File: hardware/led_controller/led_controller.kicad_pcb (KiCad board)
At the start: 2 copper layers, 50 x 70 mm, 31 parts, among them J1 Header, J2 Header, J3 Header, J4 Header, J5 POWER, J6 Conn_01x02, U1 74AHCT125, U3 Waveshare ESP32-S3/C6 Zero

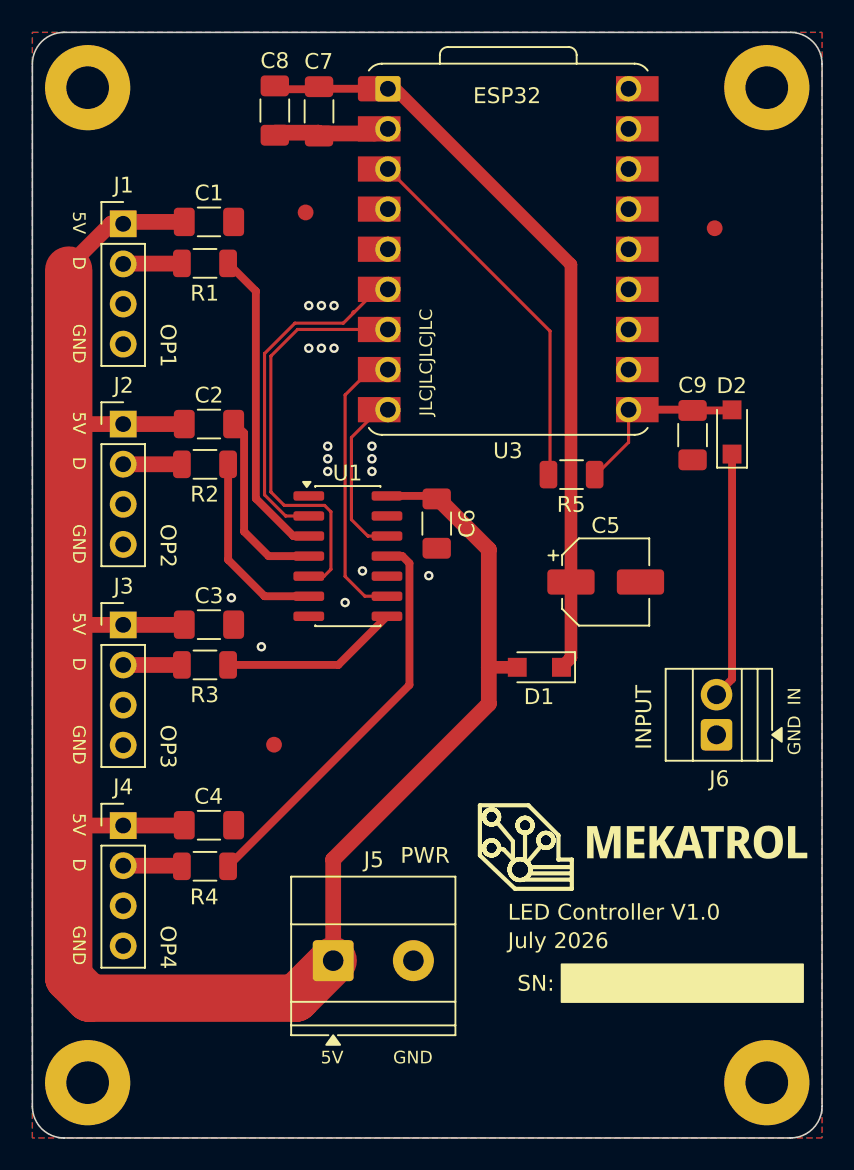
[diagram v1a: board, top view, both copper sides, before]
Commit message: Use new KICAD API in scripts
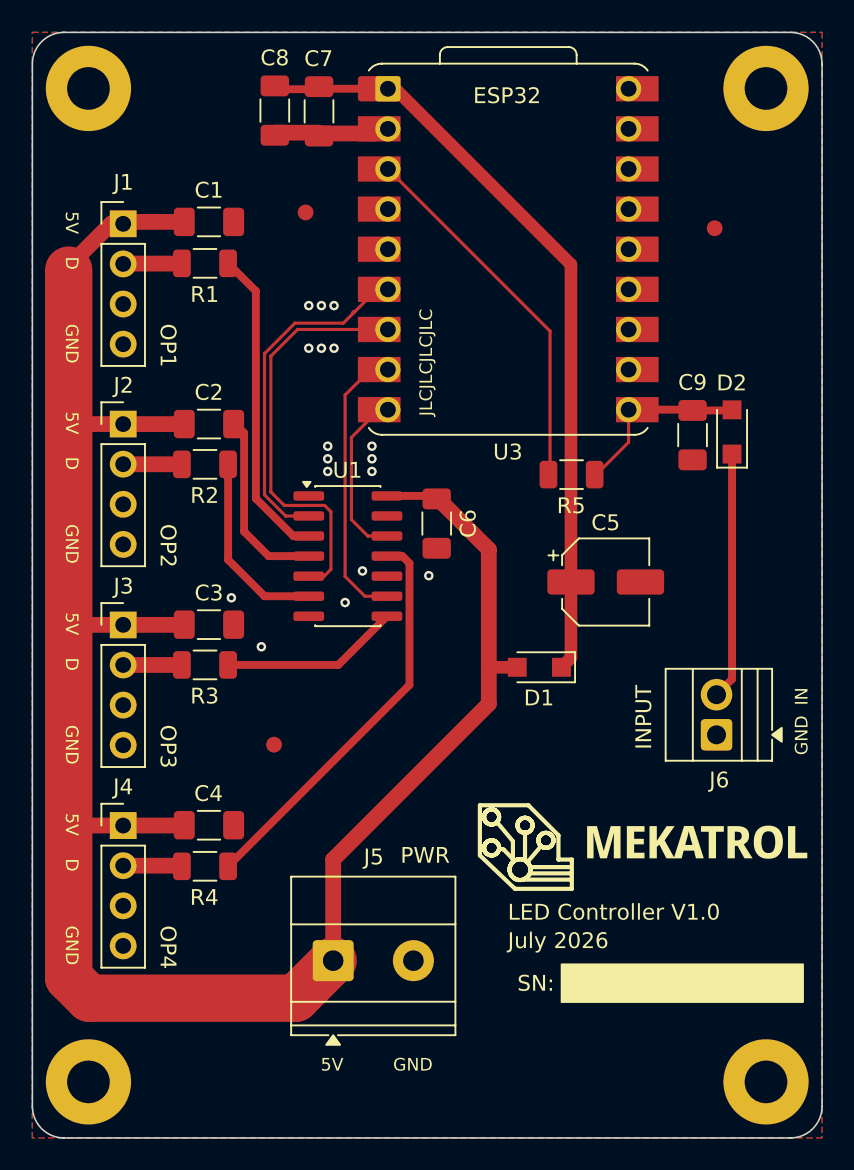
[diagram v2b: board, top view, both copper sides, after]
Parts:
- moved H2 0.07 mm to (166.4, 53.5)
- moved H4 0.07 mm to (166.4, 116.5)
- moved H1 0.07 mm to (123.5, 53.5)
- moved H3 0.07 mm to (123.5, 116.5)

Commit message: Updated center sprit to distibute as well
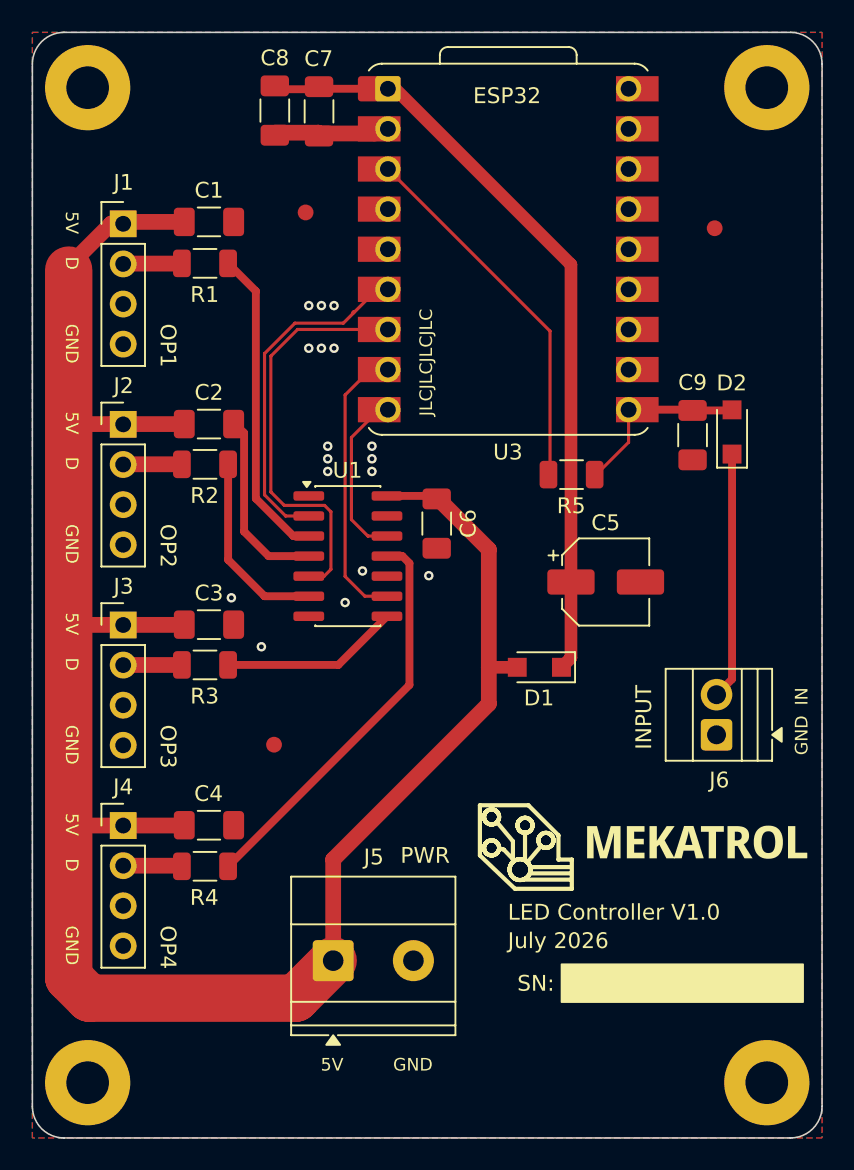
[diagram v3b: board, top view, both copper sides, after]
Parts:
- moved H2 0.07 mm to (166.5, 53.5)
- moved H4 0.07 mm to (166.5, 116.5)
- moved H1 0.07 mm to (123.5, 53.5)
- moved H3 0.07 mm to (123.5, 116.5)
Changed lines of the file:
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@@
 	(footprint "MountingHole:MountingHole_2.7mm_M2.5_Pad"
 		(layer "F.Cu")
-		(at 166.45 116.45)
+		(at 166.5 116.5)
 		(descr "Mounting Hole 2.7mm, M2.5, generated by kicad-footprint-generator mountinghole.py")
 		(tags "mountinghole M2.5")
@@
 	(footprint "Connector_PinHeader_2.54mm:PinHeader_1x04_P2.54mm_Vertical"
 		(layer "F.Cu")
-		(at 125.75 74.8)
+		(at 125.75 74.82)
 		(descr "Through hole straight pin header, 1x04, 2.54mm pitch, single row")
 		(tags "Through hole pin header THT 1x04 2.54mm single row")
@@
 		(sheetname "/")
 		(sheetfile "led_controller.kicad_sch")
-		(units
-			(unit
-				(name "A")
-				(pins "1" "2" "3" "4")
-			)
-		)
 		(attr through_hole)
 		(duplicate_pad_numbers_are_jumpers no)
@@
 	(footprint "MountingHole:MountingHole_2.7mm_M2.5_Pad"
 		(layer "F.Cu")
-		(at 166.45 53.55)
+		(at 166.5 53.5)
 		(descr "Mounting Hole 2.7mm, M2.5, generated by kicad-footprint-generator mountinghole.py")
 		(tags "mountinghole M2.5")
@@
 		(sheetname "/")
 		(sheetfile "led_controller.kicad_sch")
-		(units
-			(unit
-				(name "A")
-				(pins "1" "2" "3" "4")
-			)
-		)
 		(attr through_hole)
 		(duplicate_pad_numbers_are_jumpers no)
@@
 	(footprint "Connector_PinHeader_2.54mm:PinHeader_1x04_P2.54mm_Vertical"
 		(layer "F.Cu")
-		(at 125.75 87.513333)
+		(at 125.75 87.520001)
 		(descr "Through hole straight pin header, 1x04, 2.54mm pitch, single row")
 		(tags "Through hole pin header THT 1x04 2.54mm single row")
@@
 		(sheetname "/")
 		(sheetfile "led_controller.kicad_sch")
-		(units
-			(unit
-				(name "A")
-				(pins "1" "2" "3" "4")
-			)
-		)
 		(attr through_hole)
 		(duplicate_pad_numbers_are_jumpers no)
@@
 	(footprint "MountingHole:MountingHole_2.7mm_M2.5_Pad"
 		(layer "F.Cu")
-		(at 123.55 53.55)
+		(at 123.5 53.5)
 		(descr "Mounting Hole 2.7mm, M2.5, generated by kicad-footprint-generator mountinghole.py")
 		(tags "mountinghole M2.5")
@@
 	(footprint "MountingHole:MountingHole_2.7mm_M2.5_Pad"
 		(layer "F.Cu")
-		(at 123.55 116.45)
+		(at 123.5 116.5)
 		(descr "Mounting Hole 2.7mm, M2.5, generated by kicad-footprint-generator mountinghole.py")
 		(tags "mountinghole M2.5")

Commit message: Better messaging and unsaved file detection
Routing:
- net +3.3V: track 23.6 -> 24.5 mm, vias 0 -> 1
- net +4.6V: track 49.1 -> 48.9 mm, vias 0 -> 1

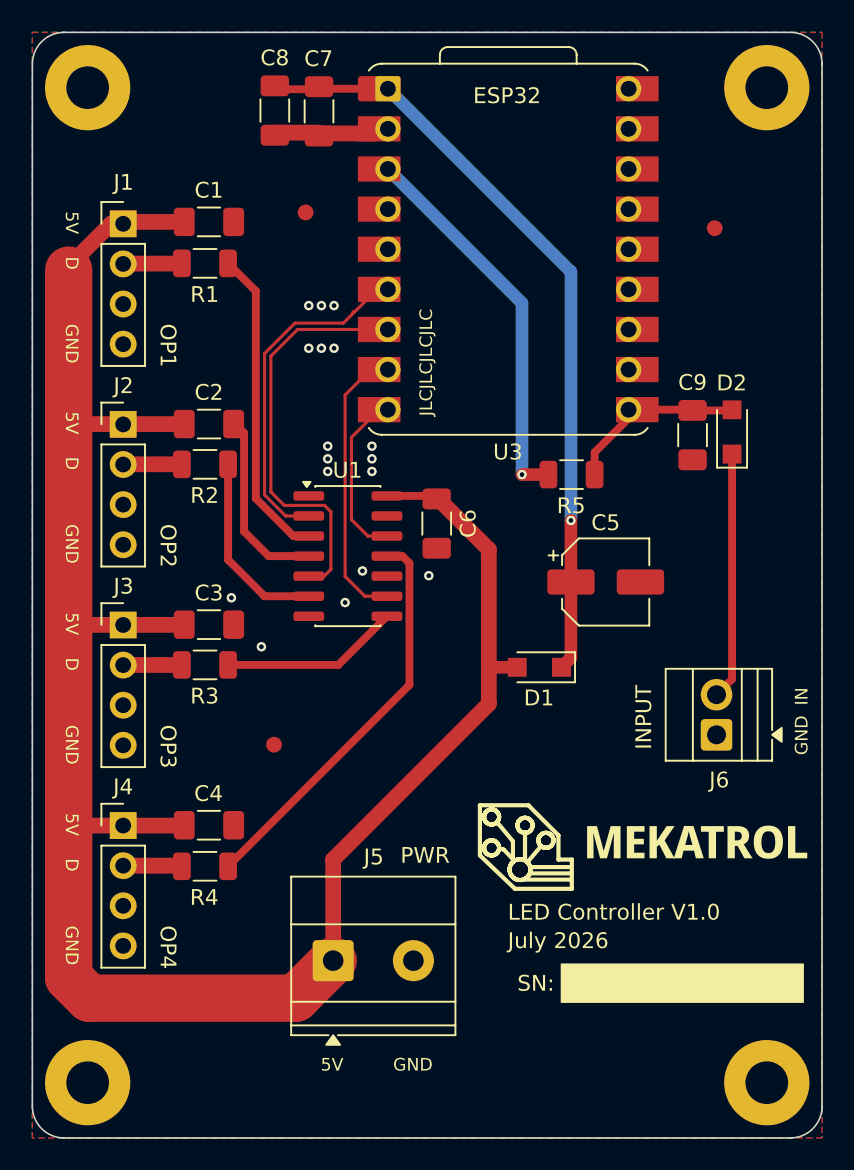
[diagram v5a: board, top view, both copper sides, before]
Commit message: Restored legacy scripts - some newer kicad bugs break API based scripts
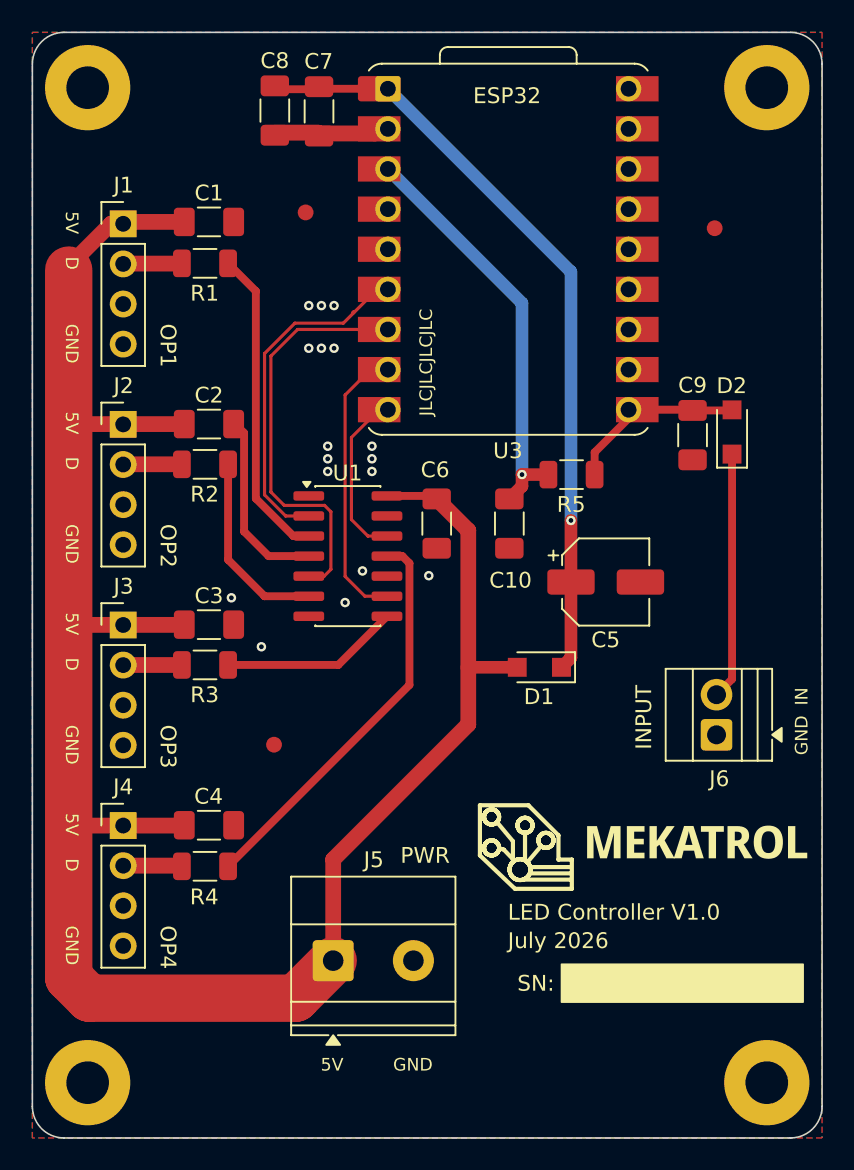
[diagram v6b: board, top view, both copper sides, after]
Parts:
- added C10: 100n, Capacitor_SMD:C_1206_3216Metric_Pad1.33x1.80mm_HandSolder, F.Cu at (150.2, 81.1)
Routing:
- net +3.3V: track 24.5 -> 26.4 mm
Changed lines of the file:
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@@
 		(tags "resistor")
 		(property "Reference" "R2"
-			(at 0.023809 -1.97825 0)
+			(at 0.023809 -1.895181 0)
 			(layer "F.SilkS")
 			(effects
@@
 		(tags "THT Terminal Block Xinya XY308-2.54-2P pitch 2.54mm size 5.58x6.5mm drill 1.2mm pad 2mm")
 		(property "Reference" "J6"
-			(at -2.86825 0.17381 180)
+			(at -2.785181 0.17381 180)
 			(layer "F.SilkS")
 			(effects
@@
 		(tags "resistor")
 		(property "Reference" "R3"
-			(at 0.023809 -1.97825 0)
+			(at 0.023809 -1.895181 0)
 			(layer "F.SilkS")
 			(effects
@@
 		(embedded_fonts no)
 	)
+	(footprint "Capacitor_SMD:C_1206_3216Metric_Pad1.33x1.80mm_HandSolder"
+		(layer "F.Cu")
+		(at 150.2 81.1 -90)
+		(descr "Capacitor SMD 1206 (3216 Metric), square (rectangular) end terminal, IPC-7351 nominal with elongated pad for handsoldering. (Body size source: IPC-SM-782 page 76, https://www.pcb-3d.com/wordpress/wp-content/uploads/ipc-sm-782a_amendment_1_and_2.pdf)")
+		(tags "capacitor handsolder")
+		(property "Reference" "C10"
+			(at 3.595 -0.075 180)
+			(layer "F.SilkS")
+			(effects
+				(font
+					(size 1 1)
+					(thickness 0.15)
+				)
+			)
+		)
+		(property "Value" "100n"
+			(at 0 1.85 90)
+			(layer "F.Fab")
+			(effects
+				(font
+					(size 1 1)
+					(thickness 0.15)
+				)
+			)
+		)
+		(property "Datasheet" ""
+			(at 0 0 90)
+			(layer "F.Fab")
+			(hide yes)
+			(effects
+				(font
+					(size 1.27 1.27)
+				)
+			)
+		)
+		(property "Description" "Unpolarized capacitor, small symbol"
+			(at 0 0 90)
+			(layer "F.Fab")
+			(hide yes)
+			(effects
+				(font
+					(size 1.27 1.27)
+				)
+			)
+		)
+		(property ki_fp_filters "C_*")
+		(sheetname "/")
+		(sheetfile "led_controller.kicad_sch")
+		(units
+			(unit
+				(name "A")
+				(pins "1" "2")
+			)
+		)
+		(attr smd)
+		(duplicate_pad_numbers_are_jumpers no)
+		(fp_line
+			(start -0.711252 0.91)
+			(end 0.711252 0.91)
+			(stroke
+				(width 0.12)
+				(type solid)
+			)
+			(layer "F.SilkS")
+		)
+		(fp_line
+			(start -0.711252 -0.91)
+			(end 0.711252 -0.91)
+			(stroke
+				(width 0.12)
+				(type solid)
+			)
+			(layer "F.SilkS")
+		)
+		(fp_rect
+			(start -2.48 -1.15)
+			(end 2.48 1.15)
+			(stroke
+				(width 0.05)
+				(type solid)
+			)
+			(fill no)
+			(layer "F.CrtYd")
+		)
+		(fp_rect
+			(start -1.6 -0.8)
+			(end 1.6 0.8)
+			(stroke
+				(width 0.1)
+				(type solid)
+			)
+			(fill no)
+			(layer "F.Fab")
+		)
+		(fp_text user "${REFERENCE}"
+			(at 0 0 90)
+			(layer "F.Fab")
+			(effects
+				(font
+					(size 0.8 0.8)
+					(thickness 0.12)
+				)
+			)
+		)
+		(pad "1" smd roundrect
+			(at -1.5625 0 270)
+			(size 1.325 1.8)
+			(layers "F.Cu" "F.Mask" "F.Paste")
+			(roundrect_rratio 0.188679)
+			(net "+3.3V")
+			(pintype "passive")
+		)
+		(pad "2" smd roundrect
+			(at 1.5625 0 270)
+			(size 1.325 1.8)
+			(layers "F.Cu" "F.Mask" "F.Paste")
+			(roundrect_rratio 0.188679)
+			(net "GND")
+			(pintype "passive")
+		)
+		(embedded_fonts no)
+		(model "${KICAD10_3DMODEL_DIR}/Capacitor_SMD.3dshapes/C_1206_3216Metric.step"
+			(offset
+				(xyz 0 0 0)
+			)
+			(scale
+				(xyz 1 1 1)
+			)
+			(rotate
+				(xyz 0 0 0)
+			)
+		)
+	)
 	(footprint "Resistor_SMD:R_1206_3216Metric"
 		(layer "F.Cu")
@@
 		(tags "resistor")
 		(property "Reference" "R5"
-			(at 0.023809 -1.97825 0)
+			(at 0.023809 -1.895181 0)
 			(layer "F.SilkS")
 			(effects
@@
 		(tags "SO SO")
 		(property "Reference" "U1"
-			(at -0.023809 -5.42825 0)
+			(at -0.023809 -5.254819 0)
 			(layer "F.SilkS")
 			(effects
@@
 		(tags "capacitor handsolder")
 		(property "Reference" "C4"
-			(at 0.023809 1.99825 180)
+			(at 0.023809 1.824818 180)
 			(layer "F.SilkS")
 			(effects
@@
 		(tags "resistor")
 		(property "Reference" "R4"
-			(at 0.047619 -1.97825 0)
+			(at 0.047619 -1.9428 0)
 			(layer "F.SilkS")
 			(effects
@@
 		(tags "capacitor electrolytic")
 		(property "Reference" "C5"
-			(at 0 -3.74825 0)
+			(at 0 3.665181 0)
 			(layer "F.SilkS")
 			(effects
@@
 		(tags "CFP3 SOD-123W")
 		(property "Reference" "D1"
-			(at 0.023809 -1.94825 180)
+			(at 0.023809 -1.865181 180)
 			(layer "F.SilkS")
 			(effects
@@
 		(tags "Through hole pin header THT 1x04 2.54mm single row")
 		(property "Reference" "J1"
-			(at 0.02381 -2.61825 0)
+			(at 0.02381 -2.444819 0)
 			(layer "F.SilkS")
 			(effects
@@
 		(tags "capacitor handsolder")
 		(property "Reference" "C1"
-			(at 0 1.99825 180)
+			(at 0 1.824819 180)
 			(layer "F.SilkS")
 			(effects
@@
 		(tags "THT Terminal Block Phoenix MKDS-1,5-2-5.08 pitch 5.08mm size 10.2x9.8mm drill 1.3mm pad 2.6mm")
 		(property "Reference" "J5"
-			(at 2.56881 -6.55825 0)
+			(at 2.56881 -6.384819 0)
 			(layer "F.SilkS")
 			(effects
@@
 		(tags "capacitor handsolder")
 		(property "Reference" "C6"
-			(at 0.000001 -1.99825 270)
+			(at -3.4 0.1 0)
 			(layer "F.SilkS")
 			(effects
@@
 		(tags "CFP3 SOD-123W")
 		(property "Reference" "D2"
-			(at 3.09825 -0.023809 180)
+			(at 2.924819 -0.023809 180)
 			(layer "F.SilkS")
 			(effects
@@
 		(tags "capacitor handsolder")
 		(property "Reference" "C8"
-			(at -3.32825 0 0)
+			(at -3.154819 0 0)
 			(layer "F.SilkS")
 			(effects
@@
 		(tags "capacitor handsolder")
 		(property "Reference" "C9"
-			(at -3.32825 0 180)
+			(at -3.154819 0 180)
 			(layer "F.SilkS")
 			(effects
@@
 		(tags "resistor")
 		(property "Reference" "R1"
-			(at 0.023809 -1.97825 0)
+			(at 0.023809 -1.895181 0)
 			(layer "F.SilkS")
 			(effects
@@
 		(tags "Waveshare ESP32 Microcontroller")
 		(property "Reference" "U3"
-			(at 7.596191 23.00825 0)
+			(at 7.596191 22.925181 0)
 			(unlocked yes)
 			(layer "F.SilkS")
@@
 		(tags "capacitor handsolder")
 		(property "Reference" "C2"
-			(at 0 1.99825 180)
+			(at 0 1.824819 180)
 			(layer "F.SilkS")
 			(effects
@@
 		(tags "capacitor handsolder")
 		(property "Reference" "C3"
-			(at 0 1.99825 180)
+			(at 0 1.824819 180)
 			(layer "F.SilkS")
 			(effects
@@
 		(tags "capacitor handsolder")
 		(property "Reference" "C7"
-			(at -3.32825 0.023809 0)
+			(at -3.154819 0.023809 0)
 			(layer "F.SilkS")
 			(effects
@@
 		(net "+3.3V")
 	)
+	(segment
+		(start 151 78.7375)
+		(end 150.2 79.5375)
+		(width 0.8)
+		(layer "F.Cu")
+		(net "+3.3V")
+	)
+	(segment
+		(start 151 78)
+		(end 151 78.7375)
+		(width 0.8)
+		(layer "F.Cu")
+		(net "+3.3V")
+	)
 	(via
 		(at 151 78)
@@
 	)
 	(segment
-		(start 139.045 108.774236)
-		(end 139.045 102.369214)
+		(start 147.6 81.5375)
+		(end 145.6 79.5375)
 		(width 1)
 		(layer "F.Cu")
@@
 	)
 	(segment
+		(start 145.4125 79.35)
+		(end 145.6 79.5375)
+		(width 0.5)
+		(layer "F.Cu")
+		(net "+5V")
+	)
+	(segment
 		(start 125.75 100.22)
 		(end 129.4175 100.22)
@@
 	)
 	(segment
-		(start 148.9 82.7375)
-		(end 145.6 79.4375)
-		(width 1)
+		(start 150.7 90.2)
+		(end 147.5 90.2)
+		(width 0.8)
 		(layer "F.Cu")
 		(net "+5V")
@@
 	)
 	(segment
-		(start 139.045 102.369214)
-		(end 148.9 92.514214)
-		(width 1)
-		(layer "F.Cu")
-		(net "+5V")
-	)
-	(segment
 		(start 122.3 109.85)
 		(end 123.6 111.15)
@@
 	)
 	(segment
-		(start 148.9 90.2)
-		(end 148.9 82.7375)
-		(width 1)
-		(layer "F.Cu")
-		(net "+5V")
-	)
-	(segment
 		(start 125.75 87.513333)
 		(end 122.013333 87.513333)
@@
 	)
 	(segment
-		(start 148.9 92.514214)
-		(end 148.9 90.2)
+		(start 147.6 93.814214)
+		(end 147.6 81.5375)
 		(width 1)
 		(layer "F.Cu")
@@
 	)
 	(segment
-		(start 145.5125 79.35)
-		(end 145.6 79.4375)
-		(width 0.5)
-		(layer "F.Cu")
-		(net "+5V")
-	)
-	(segment
 		(start 125.75 87.513333)
 		(end 129.424167 87.513333)
@@
 	)
 	(segment
-		(start 142.45 79.35)
-		(end 145.5125 79.35)
-		(width 0.5)
-		(layer "F.Cu")
-		(net "+5V")
-	)
-	(segment
 		(start 125.75 74.8)
 		(end 129.475 74.8)
@@
 	)
 	(segment
-		(start 150.7 90.2)
-		(end 148.9 90.2)
-		(width 0.8)
-		(layer "F.Cu")
-		(net "+5V")
-	)
-	(segment
 		(start 129.4175 100.22)
 		(end 129.4375 100.2)
@@
 	)
 	(segment
+		(start 142.45 79.35)
+		(end 145.4125 79.35)
+		(width 0.5)
+		(layer "F.Cu")
+		(net "+5V")
+	)
+	(segment
 		(start 123.6 111.15)
 		(end 136.669236 111.15)
@@
 		(width 1)
 		(layer "F.Cu")
+		(net "+5V")
+	)
+	(segment
+		(start 139.045 108.774236)
+		(end 139.045 102.369214)
+		(width 1)
+		(layer "F.Cu")
+		(net "+5V")
+	)
+	(segment
+		(start 139.045 102.369214)
+		(end 147.6 93.814214)
+		(width 1)
+		(layer "F.Cu")
